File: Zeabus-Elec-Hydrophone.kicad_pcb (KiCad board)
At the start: 4 copper layers, 140 x 70 mm, 352 parts, among them CN1 EPS.00.250.NTN, CN2 EPS.00.250.NTN, CN3 EPS.00.250.NTN, CN4 EPS.00.250.NTN, J1 JTAG, J10 TEST_1P, J11 TEST_1P, J12 TEST_1P, J13 TEST_1P, J14 TEST_1P, J15 TEST_1P, J16 TEST_1P, J17 TEST_1P, J18 TEST_1P, J2 USB_OTG, J22 TEST_1P, J3 TEST_1P, J4 TEST_1P, J5 TEST_1P, J6 TEST_1P, J7 TEST_1P, J8 TEST_1P, J9 TEST_1P, SW1 SW_DIP_x02, SW2 PB, SW3 PB, SW4 PB, SW5 PB, SW6 PB, U1 ADSP-21489BSWZ-4B, U10 FT232RQ, U11 AD1939WBSTZ, U12 74LVC1G08, U13 FOX924B - 12.288MHz, U14 AD8652ARZ, U15 AD8652ARZ, U16 AD8652ARZ, U17 AD8652ARZ, U18 AD8334ACPZ, U19 MAX5387LAUD+T, U2 FOX924B - 25MHz, U20 TLV73311PDBVT, U21 LM1117-3.3, U22 TLV73311PDVBT, U23 LM1117-3.3, U3 S29GL032N, U4 74LVC1G08, U5 74LVC1G08, U6 ADM708SARZ, U7 74LVC14, U8 74AC11244, U9 NCP361SNT1G, Y1 CSTCC2M00G53-R0

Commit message: Finished PCB routing. Ready for manufacture
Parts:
- R4, U2: moved to F.Cu
- moved U2 28.1 mm to (206.6, 125.7), turned to 180 degrees
- moved R4 22.3 mm to (202.6, 125.2)
- moved Y1 19.3 mm to (236.3, 120.6), turned to 90 degrees
- moved R36 4.16 mm to (207.2, 129.7)
- moved U12 4.16 mm to (204.8, 129.6)
- moved C36 1.12 mm to (226.6, 109.4)
- moved C13 1.12 mm to (226.6, 107.8)
- moved C14 1.12 mm to (226.6, 111.0)
- moved R17 0.89 mm to (236.8, 139.0), turned to 90 degrees
- moved C17 0.32 mm to (226.6, 118.7)
- moved C18 0.32 mm to (226.6, 120.3)
- moved C20 0.32 mm to (226.6, 123.5)
- moved C37 0.32 mm to (226.6, 115.5)
- moved C15 0.32 mm to (226.6, 113.9)
- moved C16 0.32 mm to (226.6, 117.1)
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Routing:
- net /DSP-Memory/A19: track 0.00 -> 163.9 mm, vias 0 -> 2
- net +3V3: track 0.00 -> 163.3 mm, vias 0 -> 30
- net /DSP-Memory/A21: track 0.00 -> 162.2 mm, vias 0 -> 2
- net /DSP-Memory/A20: track 0.00 -> 159.2 mm, vias 0 -> 2
- net /DSP-Memory/A16: track 0.00 -> 156.9 mm, vias 0 -> 2
- net /DSP-Memory/A15: track 0.00 -> 155.4 mm, vias 0 -> 2
- net /DSP-Memory/A14: track 0.00 -> 153.7 mm, vias 0 -> 2
- net /DSP-Memory/D0: track 0.00 -> 145.6 mm, vias 0 -> 4
- net /DSP-Memory/D1: track 0.00 -> 144.1 mm, vias 0 -> 4
- net /DSP-Memory/D2: track 0.00 -> 142.7 mm, vias 0 -> 4
- net ~RESET: track 0.00 -> 141.4 mm, vias 0 -> 5
- net /DSP-Memory/D3: track 0.00 -> 141.1 mm, vias 0 -> 4
- net /DSP-Memory/D4: track 0.00 -> 139.5 mm, vias 0 -> 4
- net /DSP-Memory/D5: track 0.00 -> 137.6 mm, vias 0 -> 4
- net /DSP-Memory/D6: track 0.00 -> 135.8 mm, vias 0 -> 4
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- added copper zone on B.Cu, net +1V1
- added copper zone on F.Cu, net +3.3VA
- added copper zone on F.Cu, net +3V3
- added copper zone on In2.Cu, net +3V3
- added copper zone on In2.Cu, net +5V
- added copper zone on F.Cu, net GND
- added copper zone on In1.Cu, net GND
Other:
- board size 140 x 70 mm -> 140 x 70.4 mm
- net class Default: clearance 0.16 -> 0.1524; trace_width 0.16 -> 0.1524
- rule trace_clearance: 0.16 -> 0.1524
- rule trace_min: 0.16 -> 0.1524

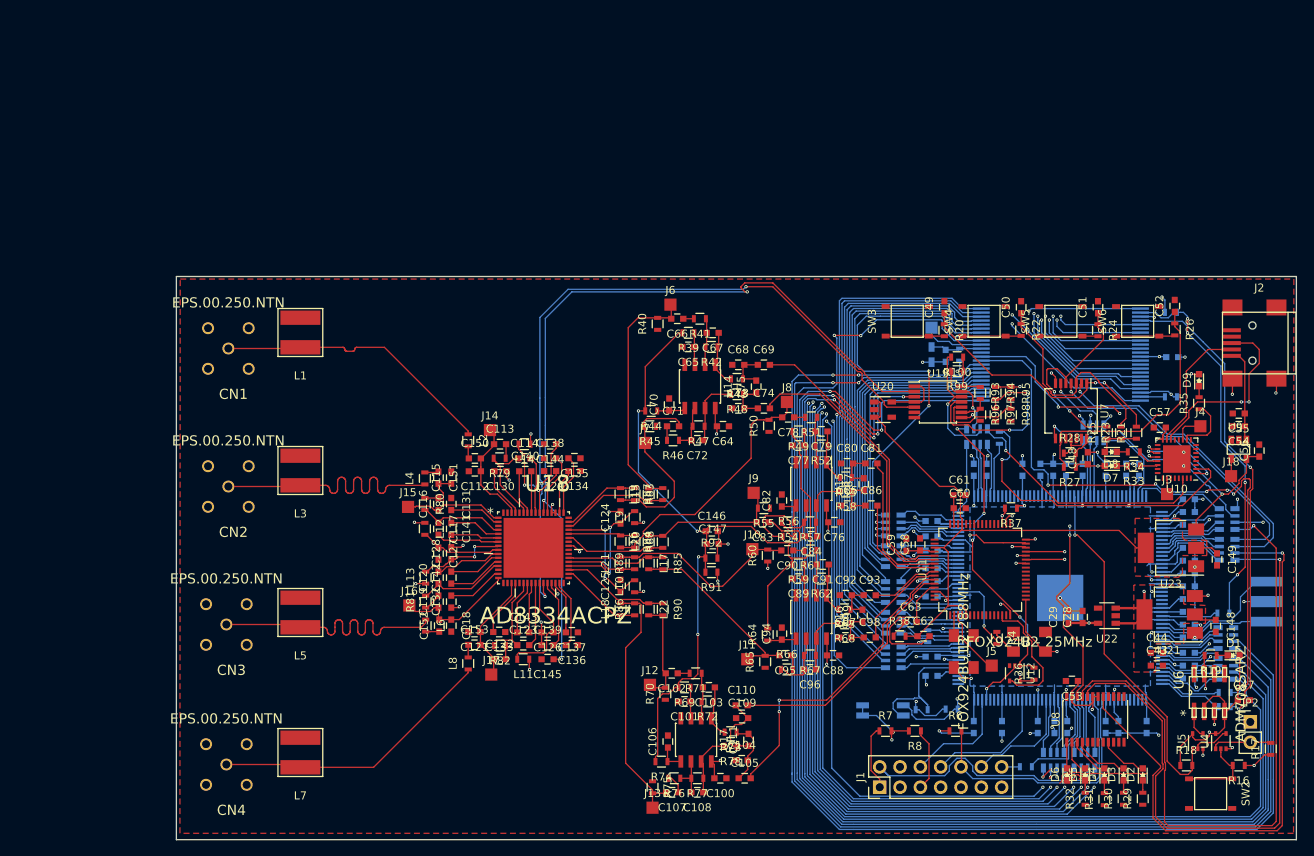
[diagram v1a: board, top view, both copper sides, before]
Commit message: Add stitched vias around analog components
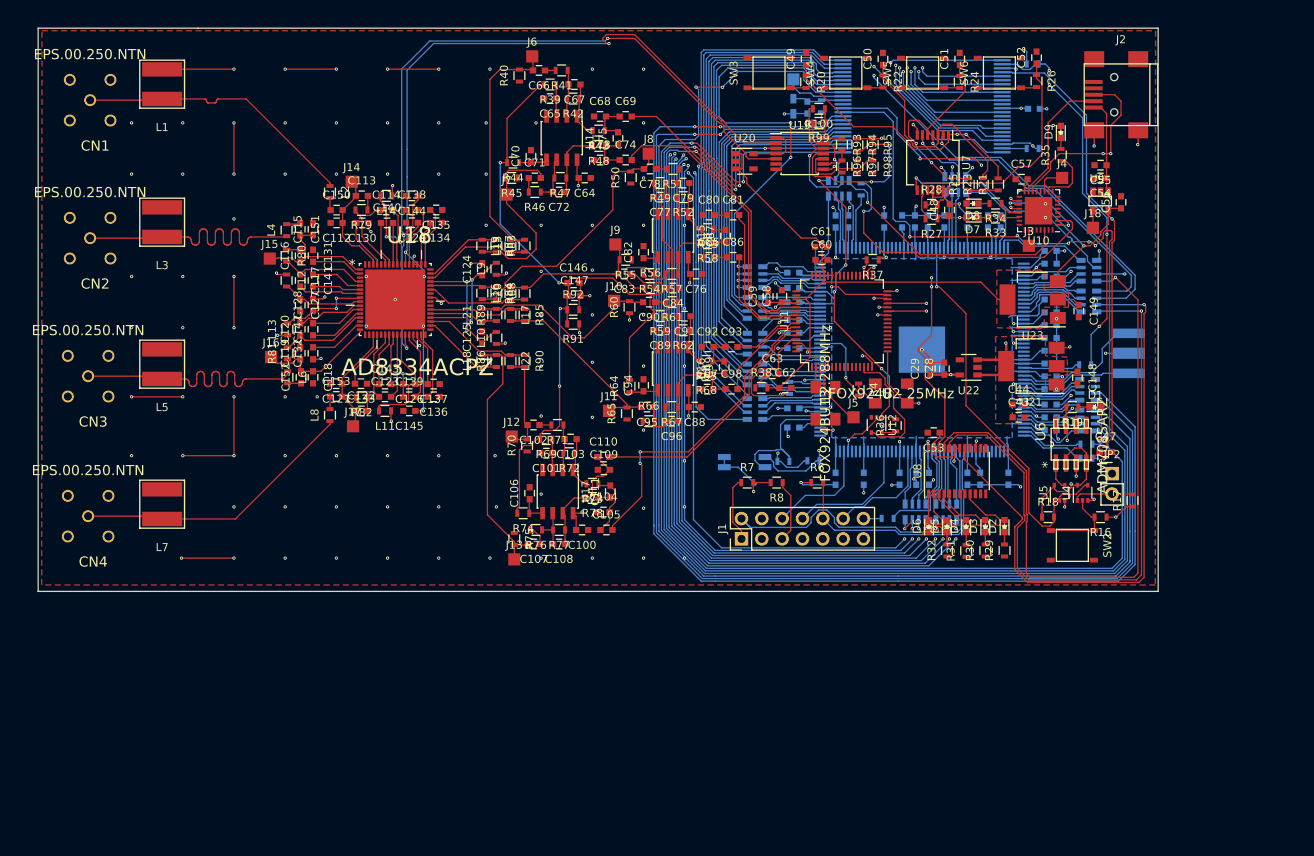
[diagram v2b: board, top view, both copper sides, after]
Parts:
- moved C103 35.5 mm to (149.3, 100.3)
- moved R69 35.5 mm to (146.2, 100.3)
- moved U8 35.5 mm to (197.6, 104.3)
- moved C115 35.5 mm to (117.1, 74.1)
- moved C118 35.5 mm to (117.1, 92.6)
- moved C128 35.5 mm to (117.1, 83.5)
- moved C132 35.5 mm to (117.1, 89.6)
- moved C140 35.5 mm to (126.3, 73.3)
- moved C141 35.5 mm to (117.1, 80.5)
- moved C142 35.5 mm to (117.1, 86.6)
- moved C143 35.5 mm to (126.1, 93.4)
- moved C152 35.5 mm to (115.6, 92.6)
- moved L11 35.5 mm to (126.1, 96.8)
- moved C101 35.5 mm to (146.2, 102.1)
- moved C112 35.5 mm to (120.0, 73.3)
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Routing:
- net GND: track 120.6 -> 808.3 mm, vias 58 -> 149

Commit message: Correction for silkscreen and add board-holding knot-hole
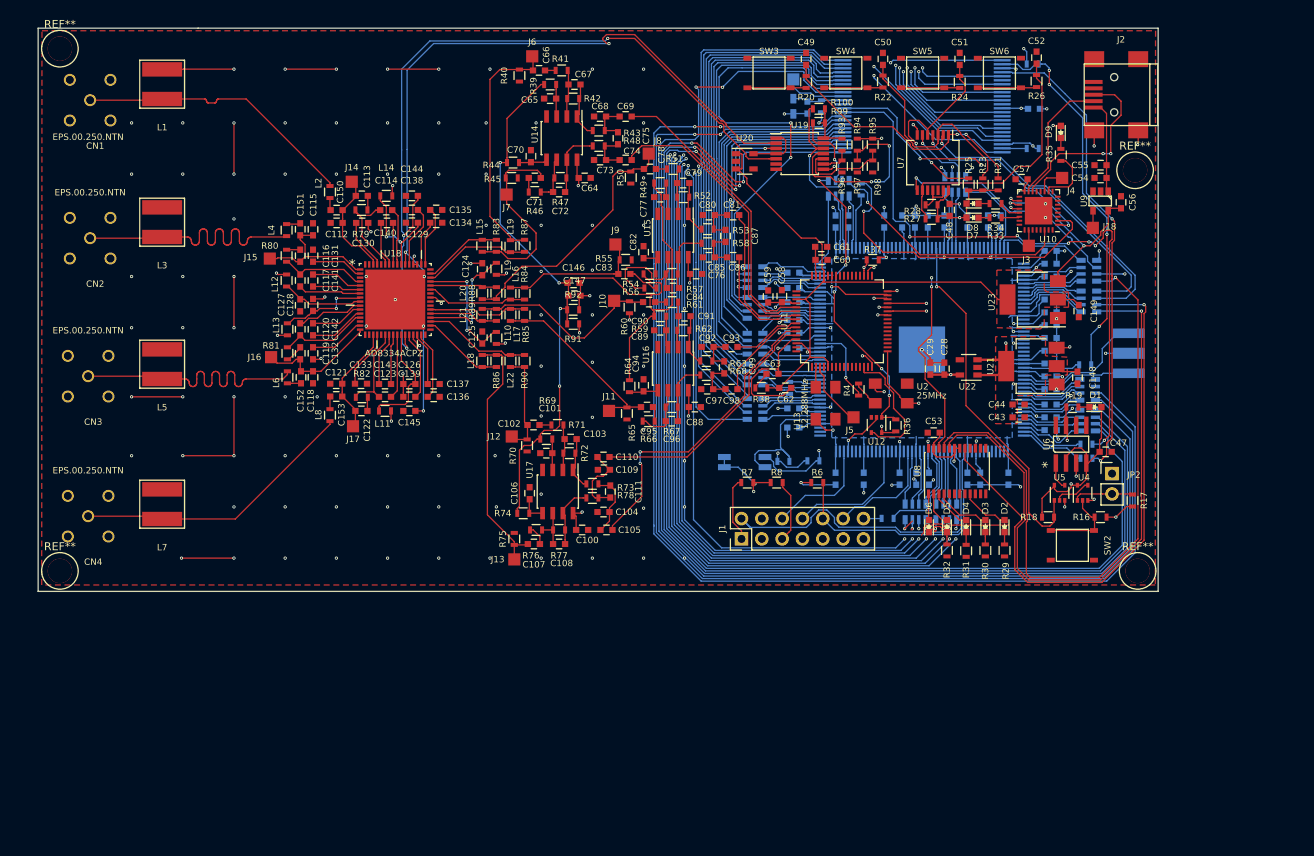
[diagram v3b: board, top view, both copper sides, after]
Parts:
- added REF**: 1pin, Connectors:1pin, F.Cu at (85.4, 116.8)
- added REF**: 1pin, Connectors:1pin, F.Cu at (85.4, 51.5)
- added REF**: 1pin, Connectors:1pin, F.Cu at (219.8, 66.7)
- added REF**: 1pin, Connectors:1pin, F.Cu at (220.2, 116.8)
- U13: value FOX924B - 12.288MHz -> 12.288MHz
- U2: value FOX924B - 25MHz -> 25MHz
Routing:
- net /DSP-External_Port/LED4: track 75.8 -> 73.1 mm
- net /DSP-External_Port/LED3: track 79.7 -> 77.1 mm
- net /DSP-External_Port/LED2: track 81.4 -> 78.9 mm
- net /DSP-Memory/A14: track 153.7 -> 152.8 mm
- net /DSP-Memory/A15: track 155.4 -> 154.4 mm
- net /DSP-Memory/A19: track 163.9 -> 162.9 mm
- net /DSP-Memory/A20: track 159.2 -> 158.2 mm
- net /DSP-Memory/A16: track 156.9 -> 156.0 mm
- net /DSP-Memory/A21: track 162.2 -> 161.3 mm
